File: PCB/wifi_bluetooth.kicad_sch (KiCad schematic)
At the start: 0 parts

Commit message: Further major components
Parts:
- added U1: ESP32-WROOM-32, RF_Module:ESP32-WROOM-32, symbol RF_Module:ESP32-WROOM-32
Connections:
- new net ESP32_VCC: U1.2 (VDD)
- new net GND: U1.1 (GND), U1.15 (GND), U1.38 (GND), U1.39 (GND)
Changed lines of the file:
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@@
 (kicad_sch (version 20230121) (generator eeschema)
   (paper "A4")
+  (wire (pts (xy 111.76 120.65) (xy 111.76 124.46))
+    (stroke (width 0) (type default))
+  )
+  (wire (pts (xy 111.76 43.18) (xy 111.76 49.53))
+    (stroke (width 0) (type default))
+  )
+  (global_label "ESP32_VCC" (shape passive) (at 111.76 43.18 90) (fields_autoplaced)
+    (effects (font (size 1.27 1.27)) (justify left))
+    (property "Intersheetrefs" "${INTERSHEET_REFS}" (at 111.76 30.7418 90)
+      (effects (font (size 1.27 1.27)) (justify left) hide)
+    )
+  )
+  (symbol (lib_id "RF_Module:ESP32-WROOM-32") (at 111.76 85.09 0) (unit 1)
+    (in_bom yes) (on_board yes) (dnp no) (fields_autoplaced)
+    (property "Reference" "U1" (at 113.7159 48.26 0)
+      (effects (font (size 1.27 1.27)) (justify left))
+    )
+    (property "Value" "ESP32-WROOM-32" (at 113.7159 50.8 0)
+      (effects (font (size 1.27 1.27)) (justify left))
+    )
+    (property "Footprint" "RF_Module:ESP32-WROOM-32" (at 111.76 123.19 0)
+      (effects (font (size 1.27 1.27)) hide)
+    )
+    (property "Datasheet" "https://www.espressif.com/sites/default/files/documentation/esp32-wroom-32_datasheet_en.pdf" (at 104.14 83.82 0)
+      (effects (font (size 1.27 1.27)) hide)
+    )
+    (pin "1")
+    (pin "10")
+    (pin "11")
+    (pin "12")
+    (pin "13")
+    (pin "14")
+    (pin "15")
+    (pin "16")
+    (pin "17")
+    (pin "18")
+    (pin "19")
+    (pin "2")
+    (pin "20")
+    (pin "21")
+    (pin "22")
+    (pin "23")
+    (pin "24")
+    (pin "25")
+    (pin "26")
+    (pin "27")
+    (pin "28")
+    (pin "29")
+    (pin "3")
+    (pin "30")
+    (pin "31")
+    (pin "32")
+    (pin "33")
+    (pin "34")
+    (pin "35")
+    (pin "36")
+    (pin "37")
+    (pin "38")
+    (pin "39")
+    (pin "4")
+    (pin "5")
+    (pin "6")
+    (pin "7")
+    (pin "8")
+    (pin "9")
+    (instances
+      (project "motor_tracker"
+        (path "/a8928dcf-7fea-46f0-8c15-a3fa49b43e6b/73fa857c-7600-465f-9c2b-9cfa1b958a36"
+          (reference "U1") (unit 1)
+        )
+      )
+    )
+  )
+  (symbol (lib_id "power:GND") (at 111.76 124.46 0) (unit 1)
+    (in_bom yes) (on_board yes) (dnp no) (fields_autoplaced)
+    (property "Reference" "#PWR01" (at 111.76 130.81 0)
+      (effects (font (size 1.27 1.27)) hide)
+    )
+    (property "Value" "GND" (at 111.76 129.54 0)
+      (effects (font (size 1.27 1.27)))
+    )
+    (property "Footprint" "" (at 111.76 124.46 0)
+      (effects (font (size 1.27 1.27)) hide)
+    )
+    (property "Datasheet" "" (at 111.76 124.46 0)
+      (effects (font (size 1.27 1.27)) hide)
+    )
+    (pin "1")
+    (instances
+      (project "motor_tracker"
+        (path "/a8928dcf-7fea-46f0-8c15-a3fa49b43e6b/73fa857c-7600-465f-9c2b-9cfa1b958a36"
+          (reference "#PWR01") (unit 1)
+        )
+      )
+    )
+  )
 )

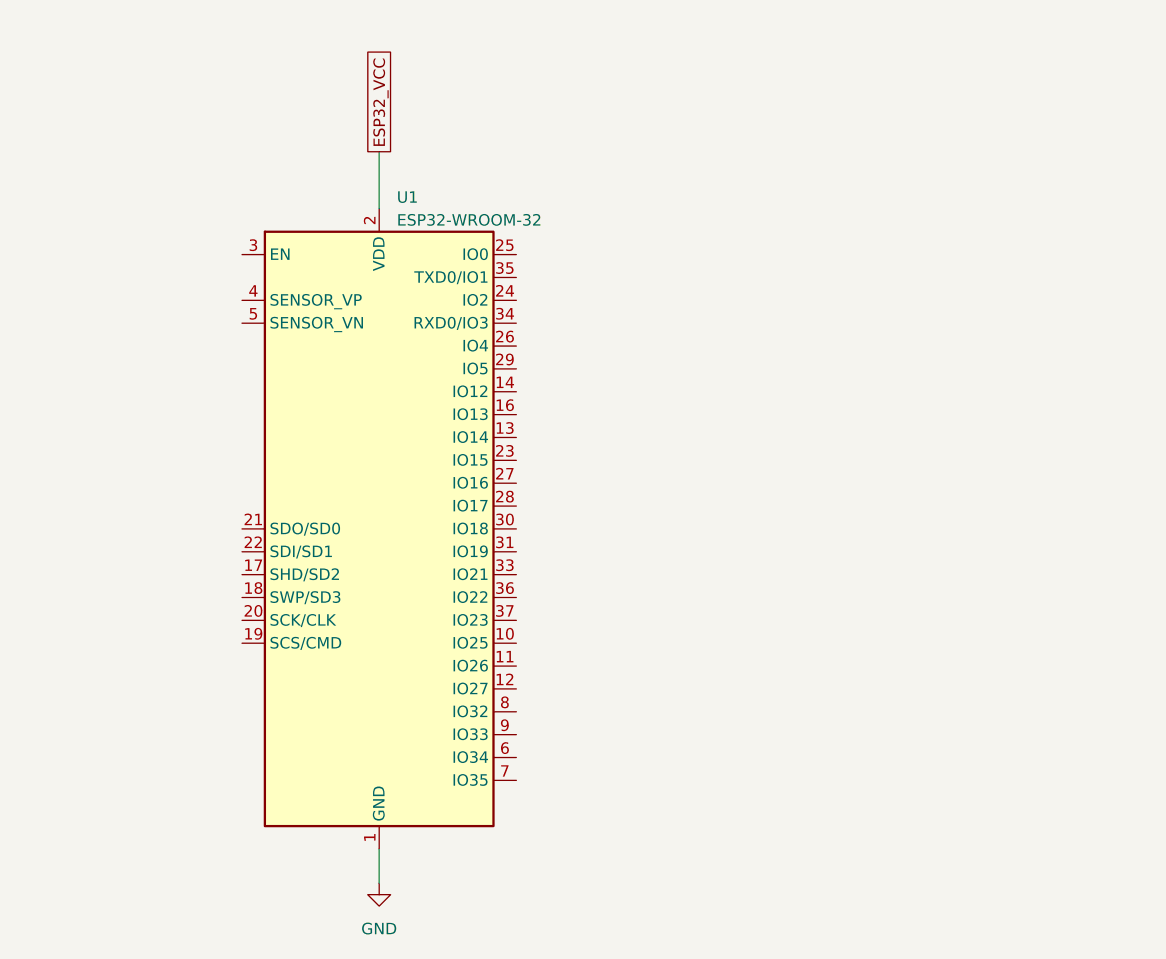
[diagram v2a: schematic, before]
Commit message: Added USB connector
Added acceleration sensor

Added combined gyro and acceleration sensor
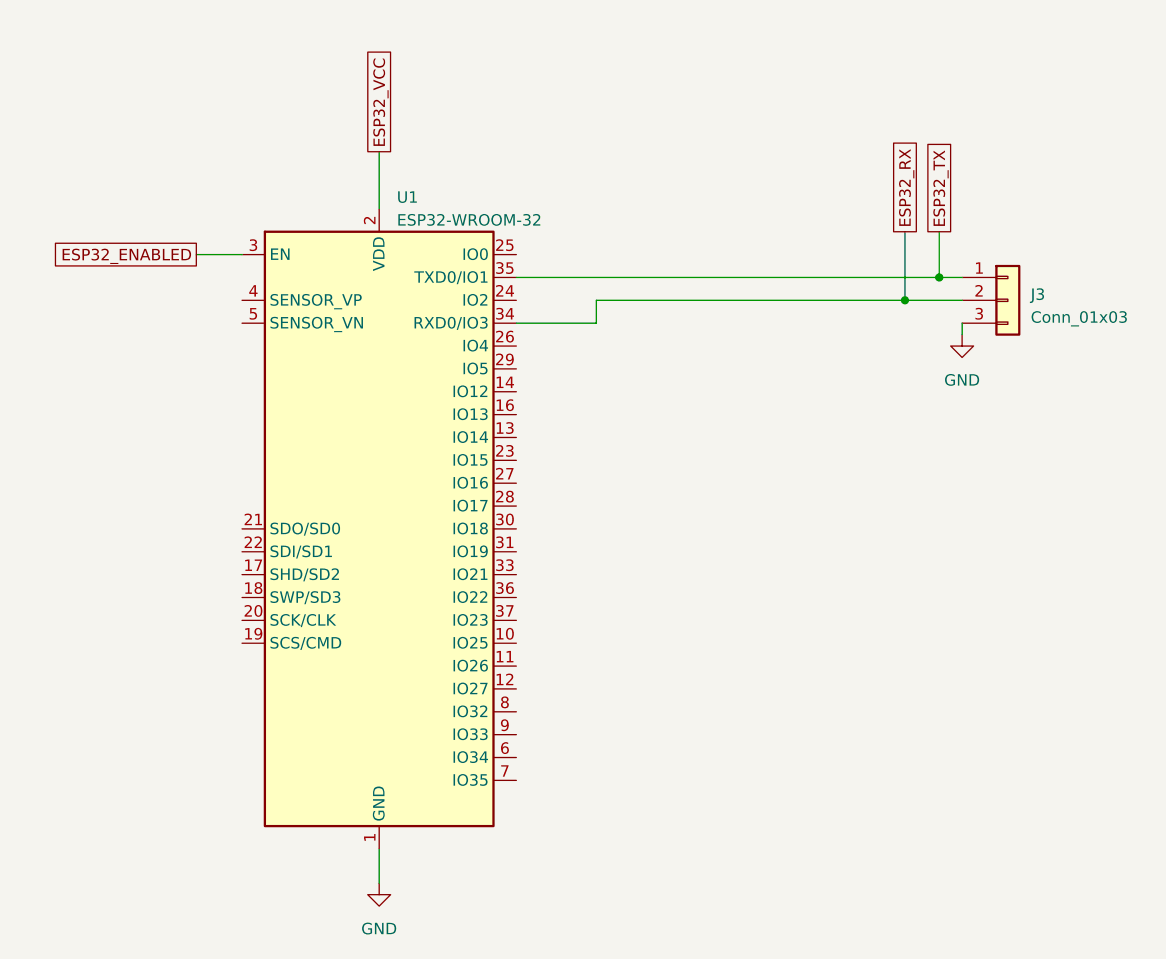
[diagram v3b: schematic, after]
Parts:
- added J3: Conn_01x03, symbol Connector_Generic:Conn_01x03
- U1: Hestore (none) -> https://www.hestore.hu/prod_10037786.html
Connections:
- net GND: now also J3.3 (Pin_3)
- net ESP32_ENABLED: now reaches U1.3 (EN)
- net ESP32_RX: now reaches U1.34 (RXD0/IO3)
- net ESP32_RX: now also J3.2 (Pin_2)
- net ESP32_TX: now reaches U1.35 (TXD0/IO1)
- net ESP32_TX: now also J3.1 (Pin_1)
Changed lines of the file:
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@@
 (kicad_sch (version 20230121) (generator eeschema)
   (paper "A4")
+  (junction (at 173.99 57.15) (diameter 0) (color 0 0 0 0)
+  )
+  (junction (at 170.18 59.69) (diameter 0) (color 0 0 0 0)
+  )
+  (wire (pts (xy 135.89 62.23) (xy 135.89 59.69))
+    (stroke (width 0) (type default))
+  )
+  (wire (pts (xy 173.99 57.15) (xy 176.53 57.15))
+    (stroke (width 0) (type default))
+  )
+  (wire (pts (xy 127 62.23) (xy 135.89 62.23))
+    (stroke (width 0) (type default))
+  )
+  (wire (pts (xy 176.53 62.23) (xy 176.53 63.5))
+    (stroke (width 0) (type default))
+  )
+  (wire (pts (xy 170.18 52.07) (xy 170.18 59.69))
+    (stroke (width 0) (type default))
+  )
+  (wire (pts (xy 135.89 59.69) (xy 170.18 59.69))
+    (stroke (width 0) (type default))
+  )
   (wire (pts (xy 111.76 120.65) (xy 111.76 124.46))
+    (stroke (width 0) (type default))
+  )
+  (wire (pts (xy 170.18 59.69) (xy 176.53 59.69))
+    (stroke (width 0) (type default))
+  )
+  (wire (pts (xy 91.44 54.61) (xy 96.52 54.61))
     (stroke (width 0) (type default))
   )
@@
     (stroke (width 0) (type default))
   )
+  (wire (pts (xy 173.99 52.07) (xy 173.99 57.15))
+    (stroke (width 0) (type default))
+  )
+  (wire (pts (xy 127 57.15) (xy 173.99 57.15))
+    (stroke (width 0) (type default))
+  )
+  (global_label "ESP32_TX" (shape passive) (at 173.99 52.07 90) (fields_autoplaced)
+    (effects (font (size 1.27 1.27)) (justify left))
+    (property "Intersheetrefs" "${INTERSHEET_REFS}" (at 173.99 41.0833 90)
+      (effects (font (size 1.27 1.27)) (justify left) hide)
+    )
+  )
   (global_label "ESP32_VCC" (shape passive) (at 111.76 43.18 90) (fields_autoplaced)
     (effects (font (size 1.27 1.27)) (justify left))
     (property "Intersheetrefs" "${INTERSHEET_REFS}" (at 111.76 30.7418 90)
       (effects (font (size 1.27 1.27)) (justify left) hide)
+    )
+  )
+  (global_label "ESP32_RX" (shape passive) (at 170.18 52.07 90) (fields_autoplaced)
+    (effects (font (size 1.27 1.27)) (justify left))
+    (property "Intersheetrefs" "${INTERSHEET_REFS}" (at 170.18 40.7809 90)
+      (effects (font (size 1.27 1.27)) (justify left) hide)
+    )
+  )
+  (global_label "ESP32_ENABLED" (shape passive) (at 91.44 54.61 180) (fields_autoplaced)
+    (effects (font (size 1.27 1.27)) (justify right))
+    (property "Intersheetrefs" "${INTERSHEET_REFS}" (at 74.3452 54.61 0)
+      (effects (font (size 1.27 1.27)) (justify right) hide)
+    )
+  )
+  (symbol (lib_id "power:GND") (at 176.53 63.5 0) (unit 1)
+    (in_bom yes) (on_board yes) (dnp no) (fields_autoplaced)
+    (property "Reference" "#PWR08" (at 176.53 69.85 0)
+      (effects (font (size 1.27 1.27)) hide)
+    )
+    (property "Value" "GND" (at 176.53 68.58 0)
+      (effects (font (size 1.27 1.27)))
+    )
+    (property "Footprint" "" (at 176.53 63.5 0)
+      (effects (font (size 1.27 1.27)) hide)
+    )
+    (property "Datasheet" "" (at 176.53 63.5 0)
+      (effects (font (size 1.27 1.27)) hide)
+    )
+    (pin "1")
+    (instances
+      (project "motor_tracker"
+        (path "/a8928dcf-7fea-46f0-8c15-a3fa49b43e6b/73fa857c-7600-465f-9c2b-9cfa1b958a36"
+          (reference "#PWR08") (unit 1)
+        )
+      )
     )
   )
@@
     )
     (property "Datasheet" "https://www.espressif.com/sites/default/files/documentation/esp32-wroom-32_datasheet_en.pdf" (at 104.14 83.82 0)
+      (effects (font (size 1.27 1.27)) hide)
+    )
+    (property "Hestore" "https://www.hestore.hu/prod_10037786.html" (at 111.76 85.09 0)
       (effects (font (size 1.27 1.27)) hide)
     )
@@
         )
       )
+    )
+  )
+  (symbol (lib_id "Connector_Generic:Conn_01x03") (at 181.61 59.69 0) (unit 1)
+    (in_bom yes) (on_board yes) (dnp no) (fields_autoplaced)
+    (property "Reference" "J3" (at 184.15 59.055 0)
+      (effects (font (size 1.27 1.27)) (justify left))
+    )
+    (property "Value" "Conn_01x03" (at 184.15 61.595 0)
+      (effects (font (size 1.27 1.27)) (justify left))
+    )
+    (property "Footprint" "" (at 181.61 59.69 0)
+      (effects (font (size 1.27 1.27)) hide)
+    )
+    (property "Datasheet" "~" (at 181.61 59.69 0)
+      (effects (font (size 1.27 1.27)) hide)
+    )
+    (pin "1")
+    (pin "2")
+    (pin "3")
+    (instances
+      (project "motor_tracker"
+        (path "/a8928dcf-7fea-46f0-8c15-a3fa49b43e6b/73fa857c-7600-465f-9c2b-9cfa1b958a36"
+          (reference "J3") (unit 1)
+        )
+      )
